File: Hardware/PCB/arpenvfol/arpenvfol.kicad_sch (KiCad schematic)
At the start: 5 parts, among them J1 Synth_power_2x5

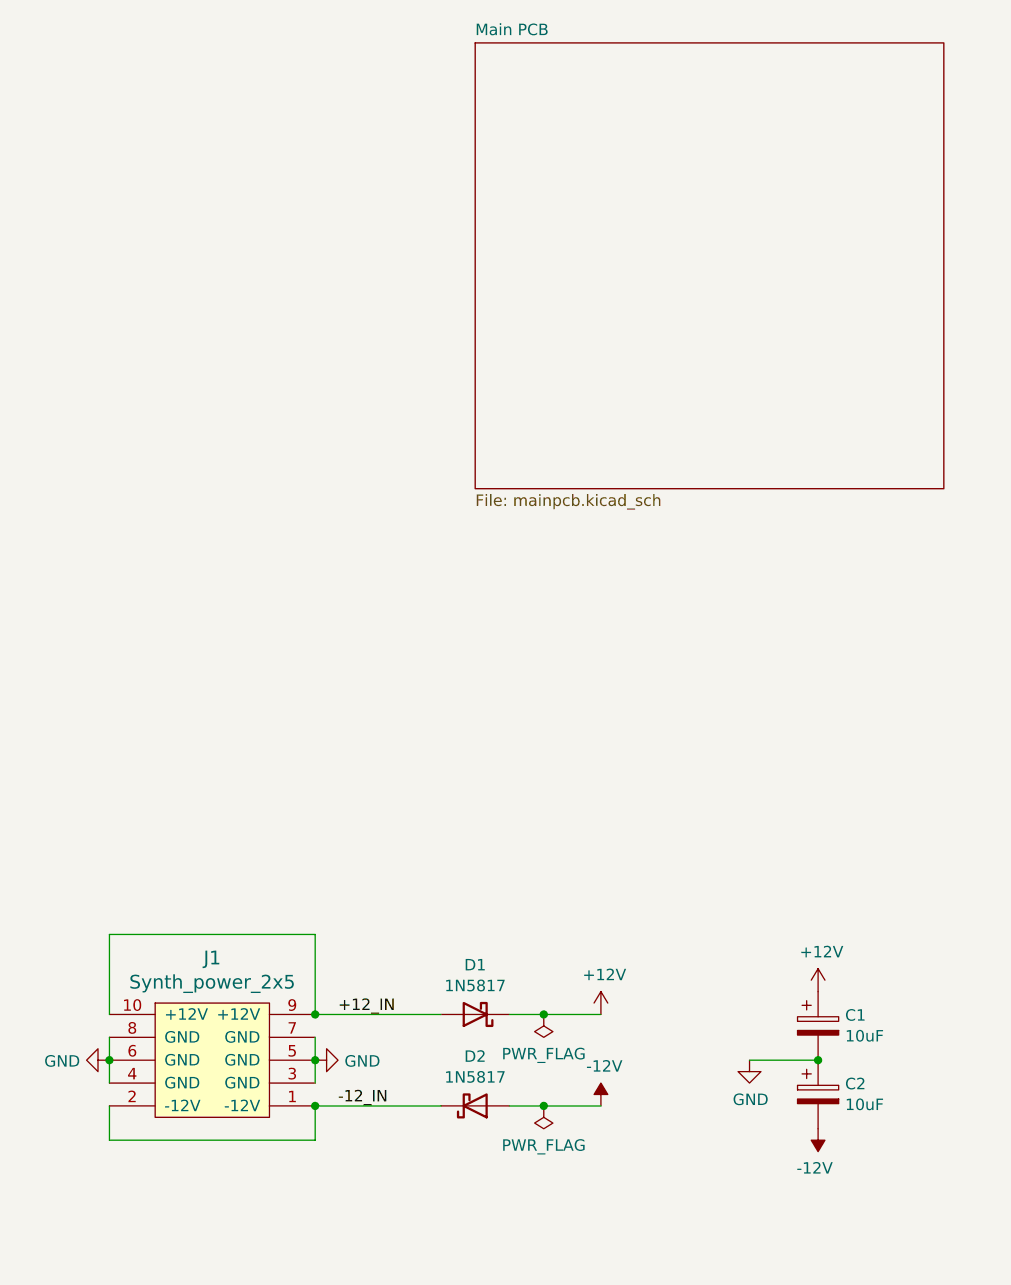
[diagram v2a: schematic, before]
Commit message: Better .gitignore; misc revisions
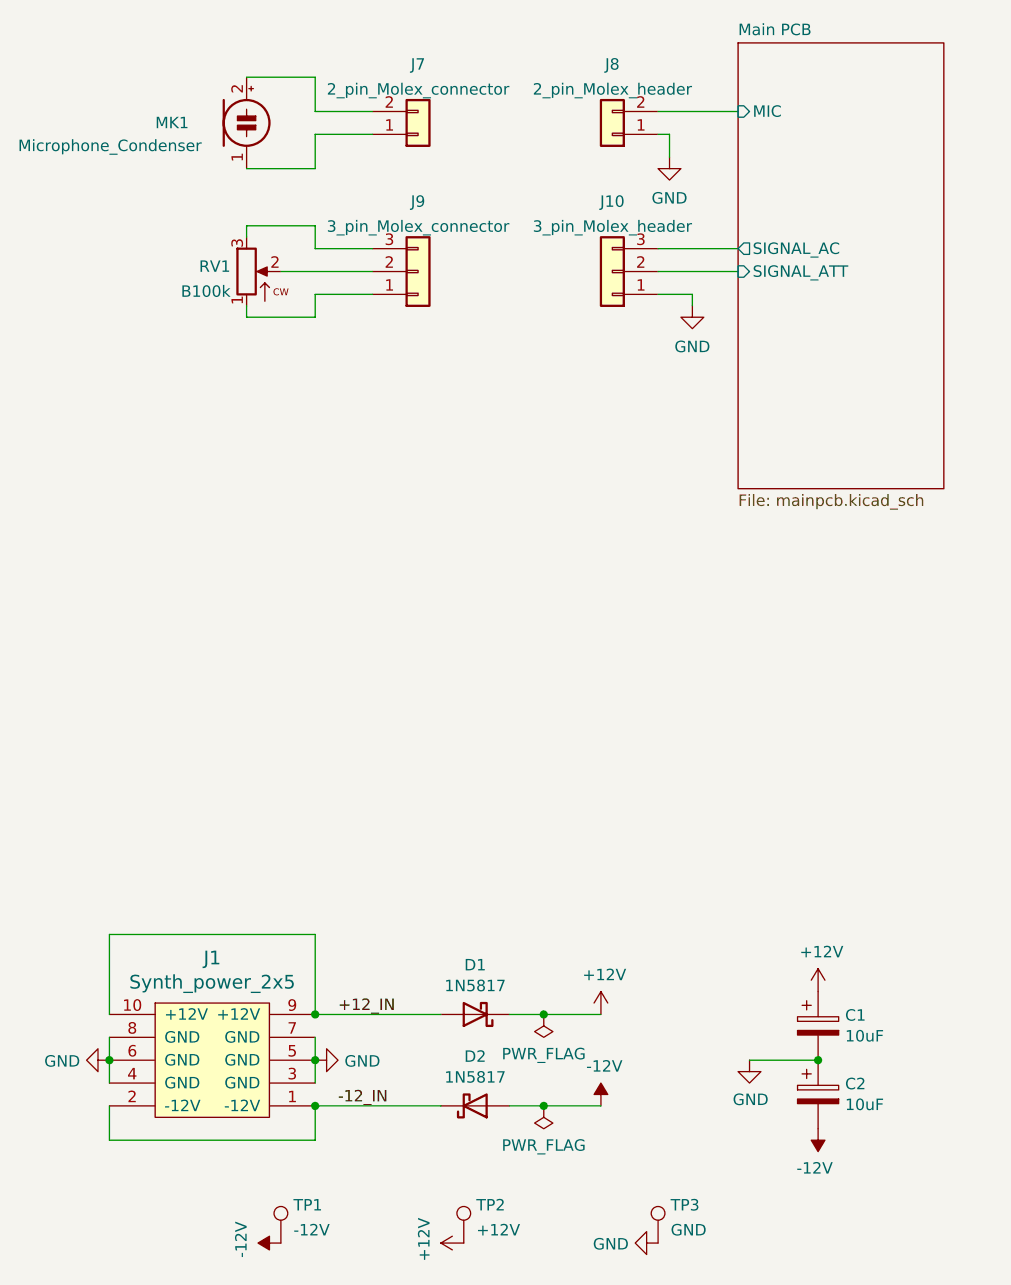
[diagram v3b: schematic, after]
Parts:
- added J10: 3_pin_Molex_header, ao_tht:Molex_KK-254_AE-6410-03A_1x03_P2.54mm_Vertical, symbol ao_symbols:3_pin_Molex_header
- added J7: 2_pin_Molex_connector, symbol ao_symbols:2_pin_Molex_connector
- added J8: 2_pin_Molex_header, ao_tht:Molex_KK-254_AE-6410-02A_1x02_P2.54mm_Vertical, symbol ao_symbols:2_pin_Molex_header
- added J9: 3_pin_Molex_connector, symbol ao_symbols:3_pin_Molex_connector
- added MK1: Microphone_Condenser, symbol Device:Microphone_Condenser
- added RV1: B100k, symbol ao_symbols:R_POT
- added TP1: -12V, ao_tht:TestPoint_THTPad_D1.5mm_Drill0.7mm, symbol ao_symbols:TestPoint
- added TP2: +12V, ao_tht:TestPoint_THTPad_D1.5mm_Drill0.7mm, symbol ao_symbols:TestPoint
- added TP3: GND, ao_tht:TestPoint_THTPad_1.5x1.5mm_Drill0.7mm, symbol ao_symbols:TestPoint
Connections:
- net +12V: now also TP2.1
- net -12V: now also TP1.1
- net GND: now also J10.1 (Pin_1), J8.1 (Pin_1), TP3.1
- new net: J7.1 (Pin_1), MK1.1 (-)
- new net: J7.2 (Pin_2), MK1.2 (+)
- new net: J9.1 (Pin_1), RV1.1
- new net: J9.2 (Pin_2), RV1.2
- new net: J9.3 (Pin_3), RV1.3
- new net Main PCB/MIC: J8.2 (Pin_2)
- new net Main PCB/SIGNAL_AC: J10.3 (Pin_3)
- new net Main PCB/SIGNAL_ATT: J10.2 (Pin_2)
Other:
- sheet Main PCB ports: added MIC, SIGNAL_AC, SIGNAL_ATT; removed none

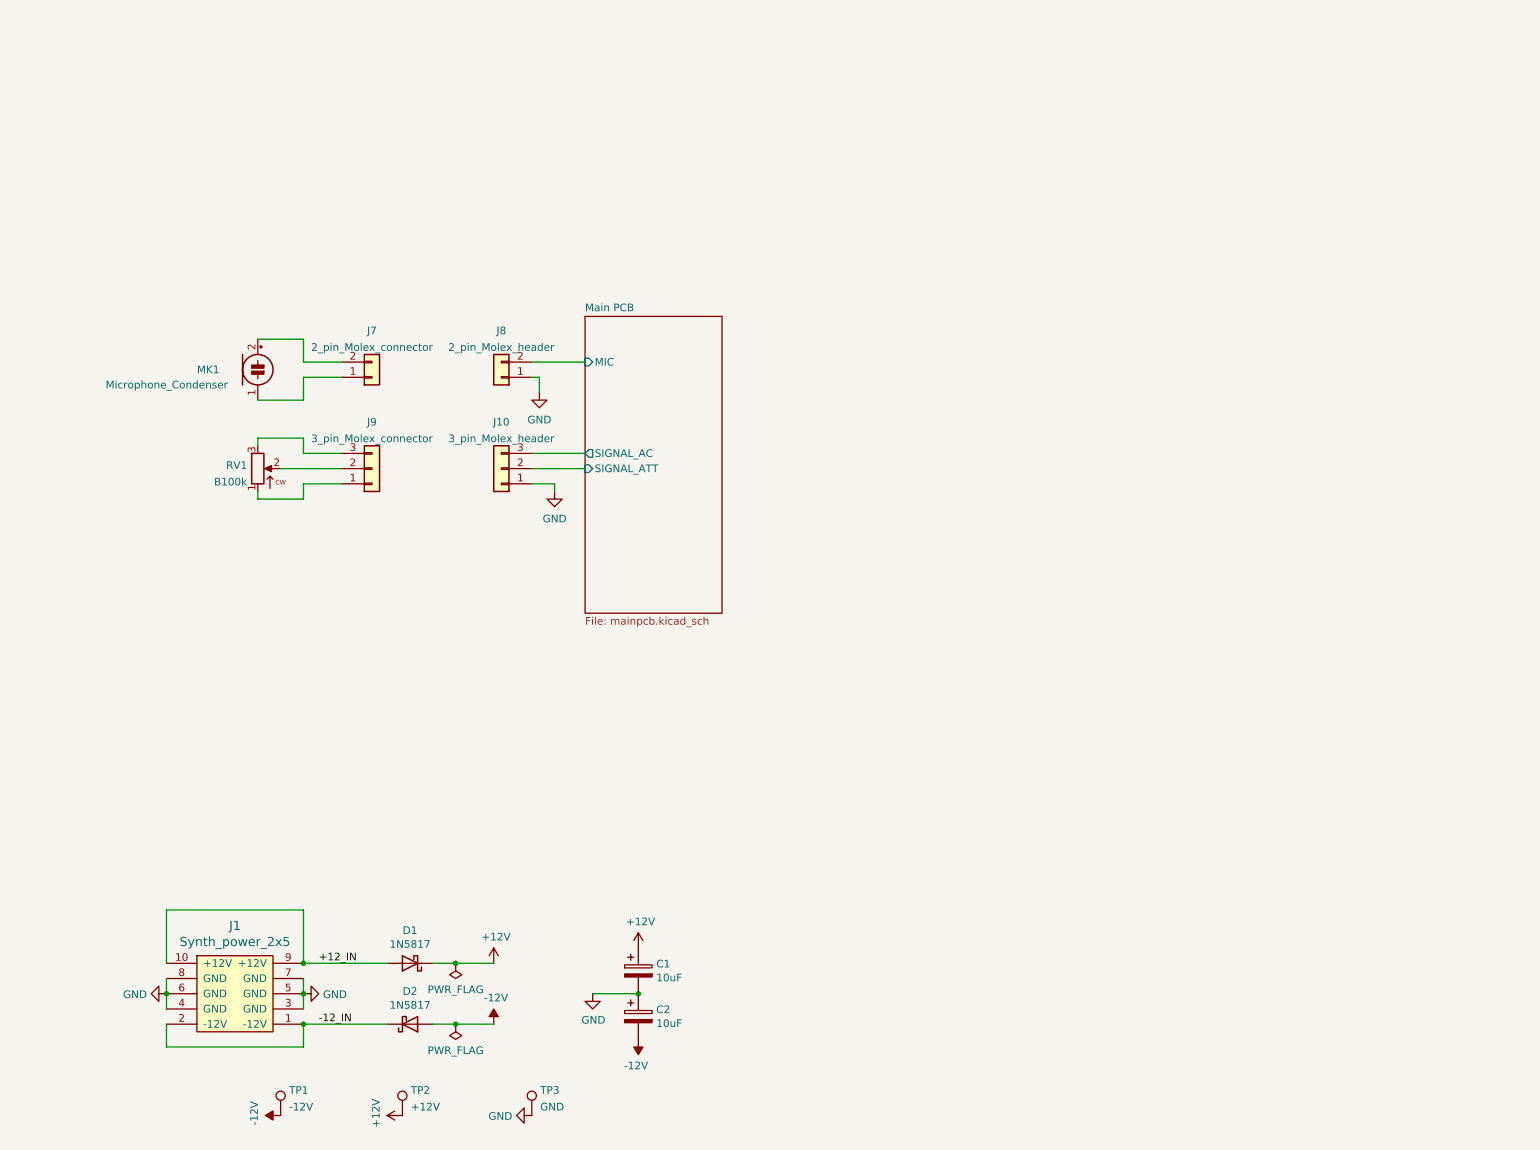
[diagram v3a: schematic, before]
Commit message: Reorganize schem; add resistor to mic preamp; change EF gain; add simulation
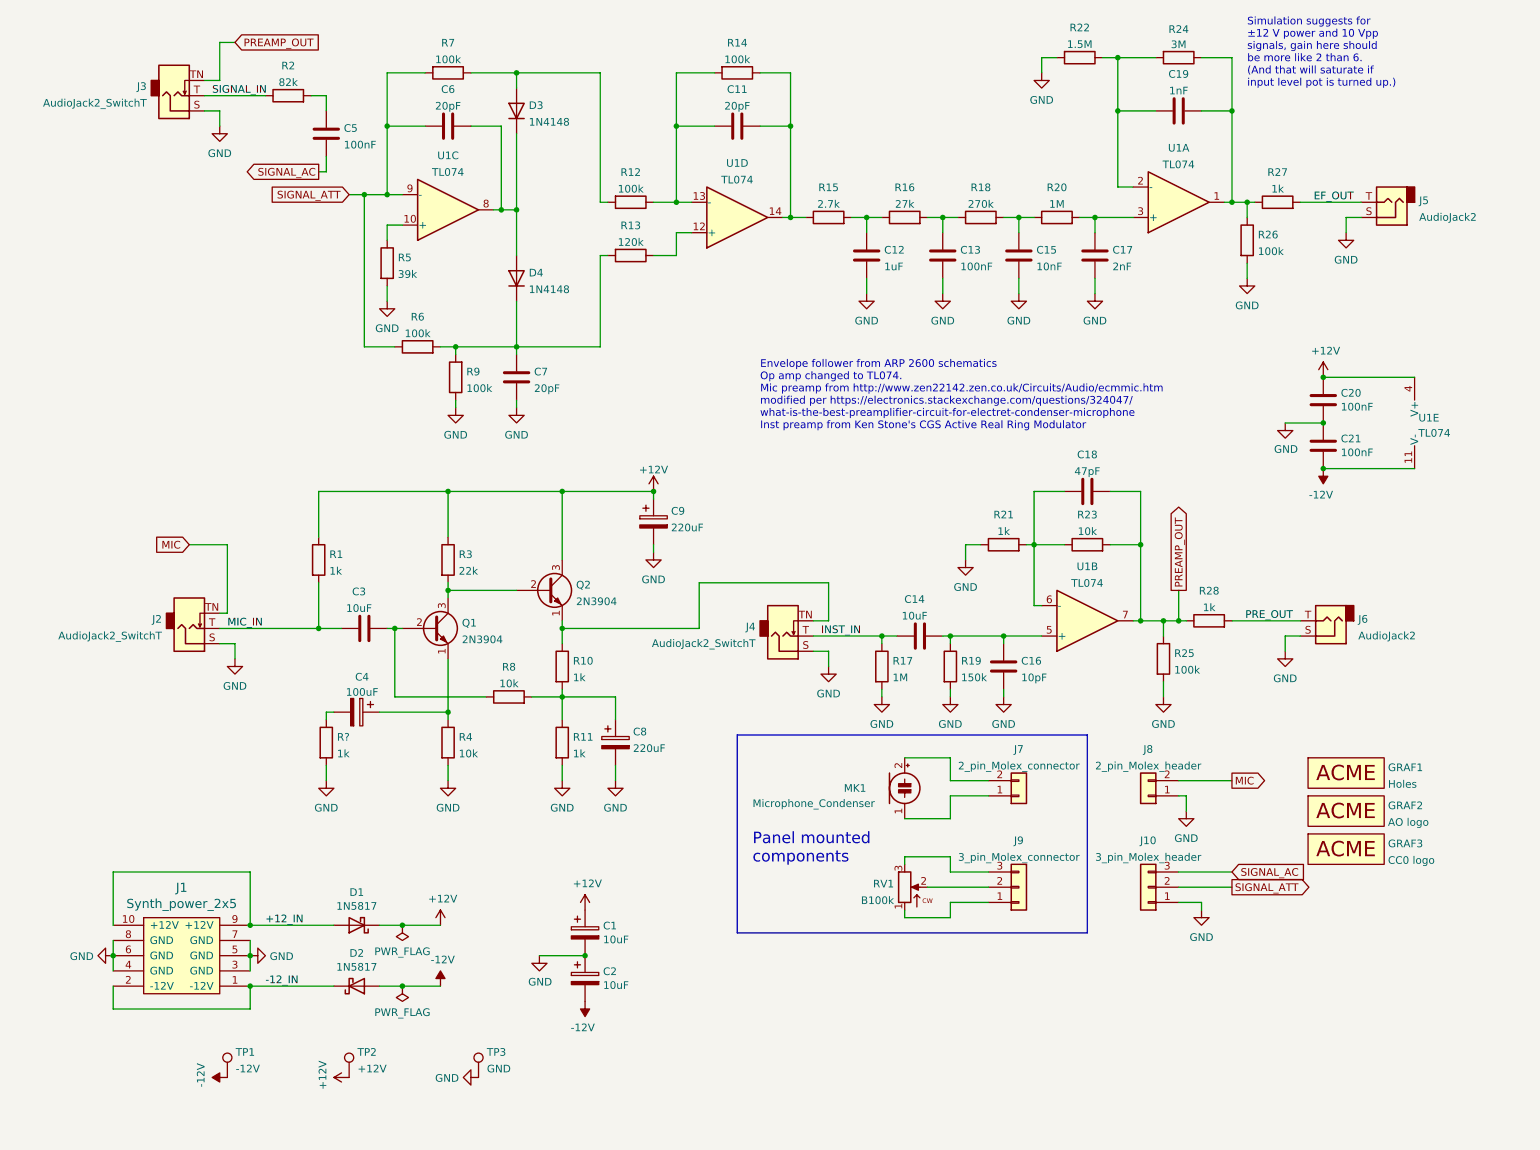
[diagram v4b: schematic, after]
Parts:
- added C11, C6, C7: 20pF, ao_tht:C_Disc_D3.0mm_W1.6mm_P2.50mm, symbol ao_symbols:C
- added C12: 1uF, ao_tht:C_Rect_L7.2mm_W2.5mm_P5.00mm_FKS2_FKP2_MKS2_MKP2, symbol ao_symbols:C
- added C13, C5: 100nF, ao_tht:C_Rect_L7.2mm_W2.5mm_P5.00mm_FKS2_FKP2_MKS2_MKP2, symbol ao_symbols:C
- added C14, C3: 10uF, ao_tht:C_Radial_D8.0mm_H11.5mm_P3.50mm, symbol ao_symbols:C
- added C15: 10nF, ao_tht:C_Rect_L7.2mm_W2.5mm_P5.00mm_FKS2_FKP2_MKS2_MKP2, symbol ao_symbols:C
- added C16: 10pF, ao_tht:C_Disc_D3.0mm_W1.6mm_P2.50mm, symbol ao_symbols:C
- added C17: 2nF, ao_tht:C_Rect_L7.2mm_W2.5mm_P5.00mm_FKS2_FKP2_MKS2_MKP2, symbol ao_symbols:C
- added C18: 47pF, ao_tht:C_Disc_D3.0mm_W1.6mm_P2.50mm, symbol ao_symbols:C
- added C19: 1nF, ao_tht:C_Rect_L7.2mm_W2.5mm_P5.00mm_FKS2_FKP2_MKS2_MKP2, symbol ao_symbols:C
- added C20, C21: 100nF, ao_tht:C_Disc_D3.0mm_W1.6mm_P2.50mm, symbol ao_symbols:C
- added C4: 100uF, ao_tht:CP_Radial_D6.3mm_P2.50mm, symbol ao_symbols:CP
- added C8, C9: 220uF, ao_tht:CP_Radial_D6.3mm_P2.50mm, symbol ao_symbols:CP
- added D3, D4: 1N4148, ao_tht:D_DO-35_SOD27_P7.62mm_Horizontal, symbol ao_symbols:1N4148
- added GRAF1: Holes, arpenvfol:arpenvfol_panel_holes, symbol ao_symbols:Graphic
- added GRAF2: AO logo, ao_tht:analogoutput_12mm, symbol ao_symbols:Graphic
- added GRAF3: CC0 logo, ao_tht:CC0_logo, symbol ao_symbols:Graphic
- added J2, J3, J4: AudioJack2_SwitchT, ao_tht:Jack_6.35mm_PJ_629HAN_slots, symbol Connector:AudioJack2_SwitchT
- added J5, J6: AudioJack2, ao_tht:Jack_6.35mm_PJ_629HAN_slots, symbol Connector:AudioJack2
- added Q1, Q2: 2N3904, ao_tht:TO-92_Inline_Wide, symbol ao_symbols:2N3904
- added R1, R10, R11, R21, R27, R28, R?: 1k, ao_tht:R_Axial_DIN0207_L6.3mm_D2.5mm_P10.16mm_Horizontal, symbol ao_symbols:R
- added R12, R14, R25, R26, R6, R7, R9: 100k, ao_tht:R_Axial_DIN0207_L6.3mm_D2.5mm_P10.16mm_Horizontal, symbol ao_symbols:R
- added R13: 120k, ao_tht:R_Axial_DIN0207_L6.3mm_D2.5mm_P10.16mm_Horizontal, symbol ao_symbols:R
- added R15: 2.7k, ao_tht:R_Axial_DIN0207_L6.3mm_D2.5mm_P10.16mm_Horizontal, symbol ao_symbols:R
- added R16: 27k, ao_tht:R_Axial_DIN0207_L6.3mm_D2.5mm_P10.16mm_Horizontal, symbol ao_symbols:R
- added R17, R20: 1M, ao_tht:R_Axial_DIN0207_L6.3mm_D2.5mm_P10.16mm_Horizontal, symbol ao_symbols:R
- added R18: 270k, ao_tht:R_Axial_DIN0207_L6.3mm_D2.5mm_P10.16mm_Horizontal, symbol ao_symbols:R
- added R19: 150k, ao_tht:R_Axial_DIN0207_L6.3mm_D2.5mm_P10.16mm_Horizontal, symbol ao_symbols:R
- added R2: 82k, ao_tht:R_Axial_DIN0207_L6.3mm_D2.5mm_P10.16mm_Horizontal, symbol ao_symbols:R
- added R22: 1.5M, ao_tht:R_Axial_DIN0207_L6.3mm_D2.5mm_P10.16mm_Horizontal, symbol ao_symbols:R
- added R23, R4, R8: 10k, ao_tht:R_Axial_DIN0207_L6.3mm_D2.5mm_P10.16mm_Horizontal, symbol ao_symbols:R
- added R24: 3M, ao_tht:R_Axial_DIN0207_L6.3mm_D2.5mm_P10.16mm_Horizontal, symbol ao_symbols:R
- added R3: 22k, ao_tht:R_Axial_DIN0207_L6.3mm_D2.5mm_P10.16mm_Horizontal, symbol ao_symbols:R
- added R5: 39k, ao_tht:R_Axial_DIN0207_L6.3mm_D2.5mm_P10.16mm_Horizontal, symbol ao_symbols:R
- added U1: TL074, ao_tht:DIP-14_W7.62mm_Socket_LongPads, symbol ao_symbols:TL074
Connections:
- net +12V: now also C20.1, C9.1, Q2.3 (C), R1.1, R3.1, U1.4 (V+)
- net -12V: now also C21.2, U1.11 (V-)
- net GND: now also C12.2, C13.2, C15.2, C16.2, C17.2, C20.2, C21.1, C7.2, C8.2, C9.2, J2.S, J3.S, J4.S, J5.S, J6.S, R11.2, R17.2, R19.2, R21.1, R22.2, R25.2, R26.2, R4.2, R5.2, R9.1, R?.2
- net Main PCB/MIC renamed MIC
- net MIC: now also J2.TN
- net Main PCB/SIGNAL_AC renamed SIGNAL_AC
- net SIGNAL_AC: now also C5.2
- net Main PCB/SIGNAL_ATT renamed SIGNAL_ATT
- net SIGNAL_ATT: now also C6.1, R6.1, R7.2, U1.9 (-)
- new net: C19.1, R22.1, R24.2, U1.2 (-)
- new net: C19.2, R24.1, R26.1, R27.1, U1.1
- new net: C14.2, C16.1, R19.1, U1.5 (+)
- new net: C7.1, D4.1 (K), R13.2, R6.2, R9.2
- new net: C5.1, R2.2
- new net: R13.1, U1.12 (+)
- new net: C11.1, R12.1, R14.2, U1.13 (-)
- new net: C11.2, R14.1, R15.1, U1.14
- new net: C8.1, R10.2, R11.1, R8.2
- new net: C15.1, R18.2, R20.1
- new net: C17.1, R20.2, U1.3 (+)
- new net: R5.1, U1.10 (+)
- new net: C6.2, D3.1 (K), D4.2 (A), U1.8
- new net: C3.2, Q1.2 (B), R8.1
- new net: C12.1, R15.2, R16.1
- new net: D3.2 (A), R12.2, R7.1
- new net: C18.1, R21.2, R23.1, U1.6 (-)
- new net: C4.1, Q1.1 (E), R4.1
- new net: Q1.3 (C), Q2.2 (B), R3.2
- new net: C13.1, R16.2, R18.1
- new net: J4.TN, Q2.1 (E), R10.1
- new net: C4.2, R?.1
- new net EF_OUT: J5.T, R27.2
- new net INST_IN: C14.1, J4.T, R17.1
- new net MIC_IN: C3.1, J2.T, R1.2
- new net PREAMP_OUT: C18.2, J3.TN, R23.2, R25.1, R28.1, U1.7
- new net PRE_OUT: J6.T, R28.2
- new net SIGNAL_IN: J3.T, R2.1
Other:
- removed sheet Main PCB
- note added: "Envelope follower from ARP 2600 schematics Op amp changed to TL074. Mic preamp from http://www.zen22142.zen.co.uk/Circuits/Audio/ecmmic.htm modified per https://electronics.stackexchange.com/questions/324047/ what-is-the-best-preamplifier-circuit-for-electret-condenser-microphone Inst preamp from Ken Stone's CGS Active Real Ring Modulator"
- note added: "Panel mounted components"
- note added: "Simulation suggests for ±12 V power and 10 Vpp signals, gain here should be more like 2 than 6. (And that will saturate if input level pot is turned up.)"
